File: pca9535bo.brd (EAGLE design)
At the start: 28.3 x 18.1 mm, 9 parts, among them IC1 PCA9535D, J1 0R, J2 0R, J3 0R

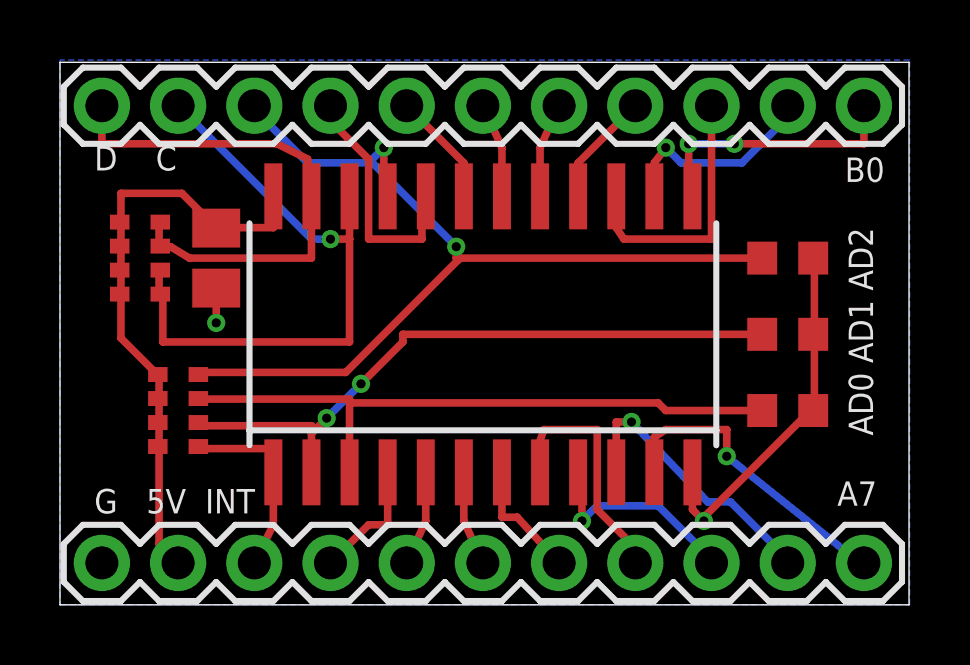
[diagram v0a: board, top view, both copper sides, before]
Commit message: the values need to be moved to the names layer to be seen...
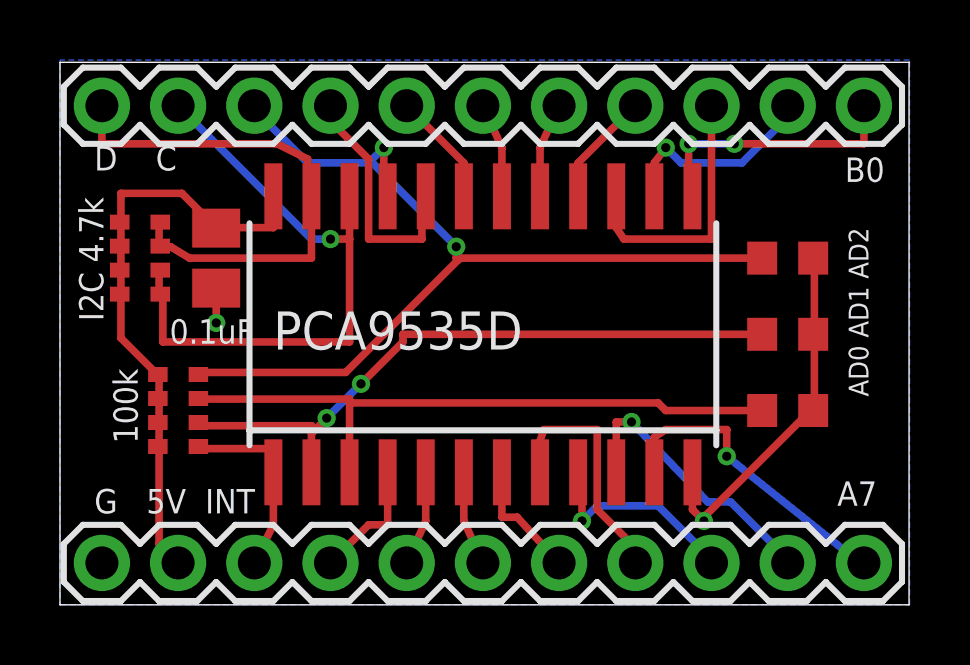
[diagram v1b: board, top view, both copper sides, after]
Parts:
- PU2: value 4.7k -> I2C 4.7k
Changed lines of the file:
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@@
 <?xml version="1.0" encoding="utf-8"?>
 <!DOCTYPE eagle SYSTEM "eagle.dtd">
-<eagle version="6.1">
+<eagle version="6.2">
 <drawing>
 <settings>
-<setting alwaysvectorfont="no"/>
+<setting alwaysvectorfont="yes"/>
 <setting verticaltext="up"/>
 </settings>
@@
 <wire x1="28.301" y1="18.085" x2="0" y2="18.085" width="0" layer="20"/>
 <wire x1="0" y1="18.085" x2="0" y2="0" width="0" layer="20"/>
-<text x="26.289" y="12.573" size="0.8128" layer="25" rot="R270">AD0 AD1 AD2</text>
-<text x="25.908" y="3.302" size="0.8128" layer="25">A7</text>
+<text x="26.289" y="12.573" size="0.6604" layer="25" font="vector" rot="R270">AD0 AD1 AD2</text>
+<text x="25.908" y="3.302" size="0.8128" layer="25" font="vector">A7</text>
 <text x="1.143" y="14.478" size="0.8128" layer="25">D    C</text>
-<text x="1.143" y="3.048" size="0.8128" layer="25">G   5V  INT</text>
-<text x="27.559" y="14.351" size="0.8128" layer="26" rot="MR0">B0   B1    B2   B3    B4    B5    B6    B7  ADR0 SCL SDA</text>
+<text x="1.143" y="3.048" size="0.8128" layer="25" font="vector">G   5V  INT</text>
+<text x="27.559" y="14.351" size="0.5334" layer="26" font="vector" rot="MR0">B0   B1    B2   B3    B4    B5    B6    B7  ADR0 SCL SDA</text>
 <text x="26.162" y="14.097" size="0.8128" layer="25">B0</text>
-<text x="27.178" y="3.175" size="0.8128" layer="26" rot="MR0">A7   A6   A5    A4   A3    A2    A1    A0   INT   5V   GND</text>
+<text x="27.178" y="3.175" size="0.508" layer="26" font="vector" rot="MR0">A7   A6   A5    A4   A3    A2    A1    A0   INT   5V   GND</text>
 </plain>
 <attributes>
@@
 <attribute name="MF" value="" x="14.097" y="9.017" size="1.778" layer="27" display="off"/>
 <attribute name="OC_FARNELL" value="1408295" x="14.097" y="9.017" size="1.778" layer="27" display="off"/>
-<attribute name="VALUE" x="7.112" y="8.509" size="1.27" layer="27"/>
+<attribute name="VALUE" x="7.112" y="8.509" size="1.27" layer="25" font="vector"/>
 </element>
 <element name="PA" library="SparkFun" package="1X11" value="M11PTH" x="1.397" y="1.397" smashed="yes"/>
@@
 <attribute name="MF" value="" x="3.937" y="6.477" size="1.778" layer="27" rot="R270" display="off"/>
 <attribute name="OC_FARNELL" value="unknown" x="3.937" y="6.477" size="1.778" layer="27" rot="R270" display="off"/>
-<attribute name="VALUE" x="1.397" y="8.382" size="1.27" layer="27" ratio="10" rot="R270"/>
+<attribute name="VALUE" x="1.778" y="7.874" size="0.8128" layer="25" font="vector" ratio="10" rot="R270"/>
 </element>
 <element name="C1" library="rcl" package="C0805K" value="0.1uF" x="5.207" y="11.557" smashed="yes" rot="R270">
-<attribute name="VALUE" x="6.207" y="9.647" size="1.016" layer="27" rot="R180"/>
+<attribute name="VALUE" x="6.461" y="9.52" size="0.8128" layer="25" font="vector" rot="R180"/>
 </element>
 <element name="J1" library="resistor" package="R0603" value="0R" x="24.257" y="11.557" smashed="yes"/>
 <element name="J2" library="resistor" package="R0603" value="0R" x="24.257" y="6.477" smashed="yes"/>
 <element name="J3" library="resistor" package="R0603" value="0R" x="24.257" y="9.017" smashed="yes"/>
-<element name="PU2" library="resistor-dil" package="CAY16" value="4.7k" x="2.667" y="11.557" smashed="yes" rot="R270">
+<element name="PU2" library="resistor-dil" package="CAY16" value="I2C 4.7k" x="2.667" y="11.557" smashed="yes" rot="R270">
 <attribute name="OC_NEWARK" value="unknown" x="2.667" y="11.557" size="1.143" layer="27" rot="R270" display="off"/>
 <attribute name="MPN" value="" x="2.667" y="11.557" size="1.143" layer="27" rot="R270" display="off"/>
 <attribute name="MF" value="" x="2.667" y="11.557" size="1.143" layer="27" rot="R270" display="off"/>
 <attribute name="OC_FARNELL" value="unknown" x="2.667" y="11.557" size="1.143" layer="27" rot="R270" display="off"/>
-<attribute name="VALUE" x="0.127" y="13.462" size="1.27" layer="27" ratio="10" rot="R270"/>
+<attribute name="VALUE" x="0.635" y="13.589" size="0.8128" layer="25" font="vector" ratio="10" rot="R270"/>
 </element>
 </elements>
